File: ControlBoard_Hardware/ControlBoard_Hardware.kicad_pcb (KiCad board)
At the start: 2 copper layers, 96.5 x 66 mm, 52 parts, among them U10 MCP1415, U11 TSR_1-2450, U2 TSR_1-2450, U3 MCP1415, U4 OKI-78SR-12, U6 MCP1415, U7 MCP1415, U8 MCP1415, U9 MCP1415

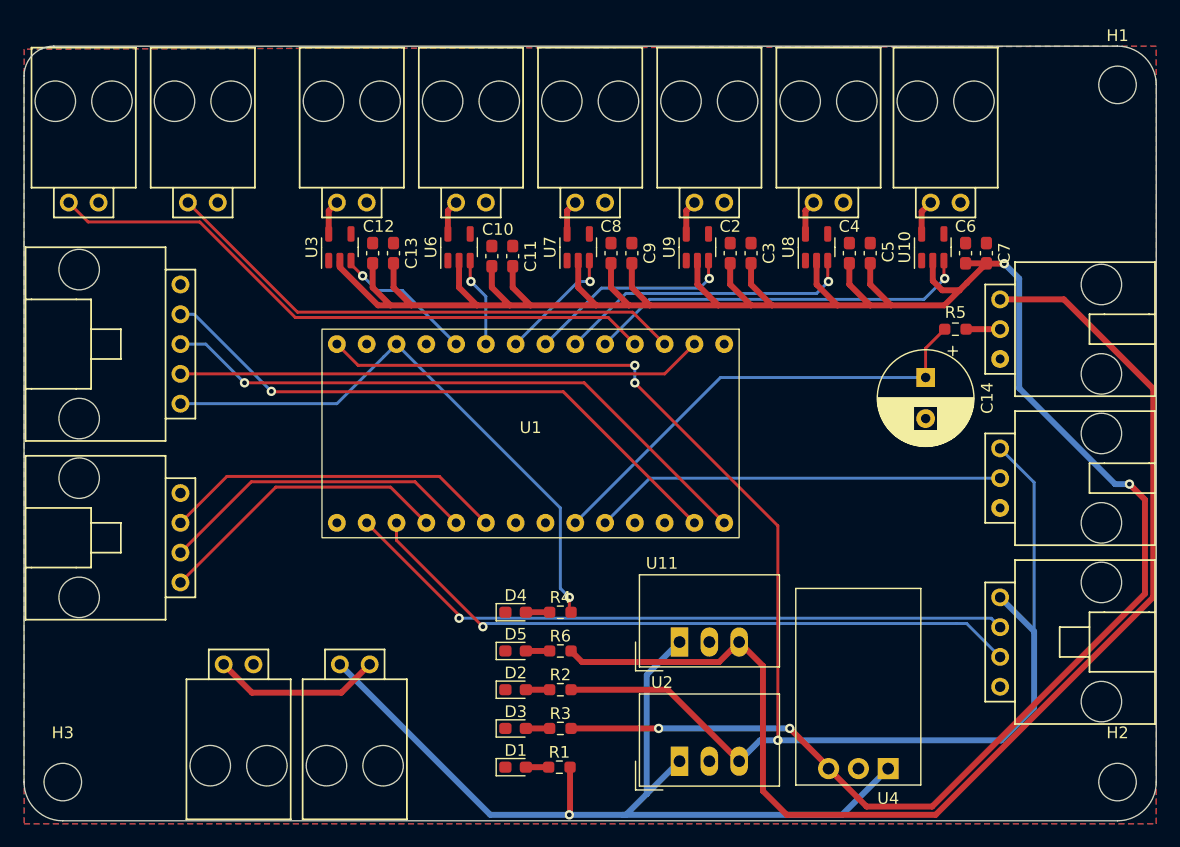
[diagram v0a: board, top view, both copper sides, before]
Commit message: Added silk screens
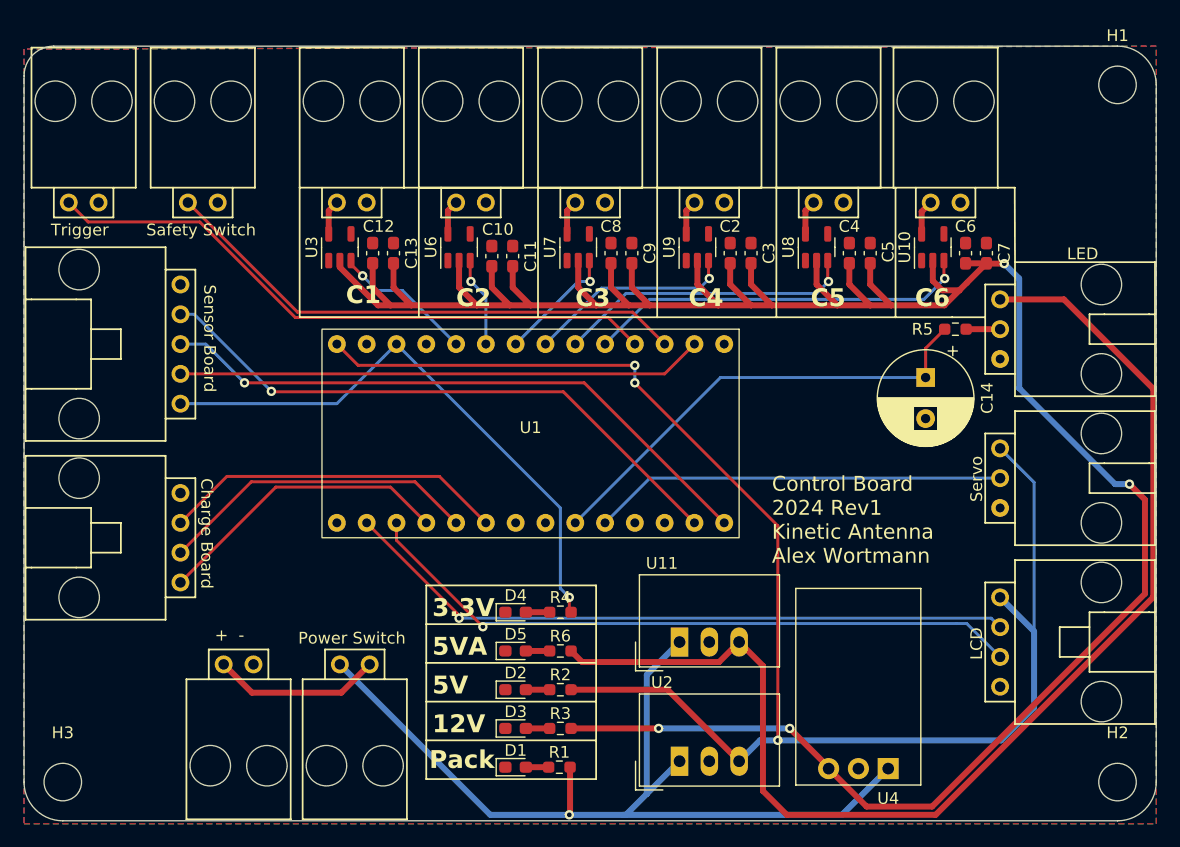
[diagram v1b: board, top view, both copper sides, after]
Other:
- board text added: "+ -"
- board text added: "12V"
- board text added: "3.3V"
- board text added: "5V"
- board text added: "5VA"
- board text added: "C1"
- board text added: "C2"
- board text added: "C3"
- board text added: "C4"
- board text added: "C5"
- board text added: "C6"
- board text added: "Charge Board"
- board text added: "Control Board 2024 Rev1 Kinetic Antenna Alex Wortmann"
- board text added: "LCD"
- board text added: "LED"
- board text added: "Pack"
- board text added: "Power Switch"
- board text added: "Safety Switch"
- board text added: "Sensor Board"
- board text added: "Servo"
- board text added: "Trigger"
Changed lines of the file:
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@@
     (property "ki_keywords" "R res resistor")
     (attr smd)
-    (fp_text reference "R5" (at 0 -1.43) (layer "F.SilkS")
+    (fp_text reference "R5" (at -2.8175 0) (layer "F.SilkS")
         (effects (font (size 1 1) (thickness 0.15)))
     )
@@
     )
   )
+  (gr_line (start 150.495 47.625) (end 150.495 58.674)
+    (stroke (width 0.15) (type default)) (layer "F.SilkS"))
+  (gr_line (start 170.815 47.625) (end 170.815 58.674)
+    (stroke (width 0.15) (type default)) (layer "F.SilkS"))
+  (gr_line (start 165.608 81.534) (end 151.13 81.534)
+    (stroke (width 0.15) (type default)) (layer "F.SilkS"))
+  (gr_line (start 165.608 98.044) (end 165.608 81.534)
+    (stroke (width 0.15) (type default)) (layer "F.SilkS"))
+  (gr_line (start 195.961 58.674) (end 198.755 58.674)
+    (stroke (width 0.15) (type default)) (layer "F.SilkS"))
+  (gr_line (start 165.608 94.742) (end 151.13 94.742)
+    (stroke (width 0.15) (type default)) (layer "F.SilkS"))
+  (gr_line (start 201.3185 53.975) (end 201.295 47.625)
+    (stroke (width 0.15) (type default)) (layer "F.SilkS"))
+  (gr_line (start 165.608 91.44) (end 151.13 91.44)
+    (stroke (width 0.15) (type default)) (layer "F.SilkS"))
+  (gr_line (start 199.848698 47.625) (end 201.295 47.625)
+    (stroke (width 0.15) (type default)) (layer "F.SilkS"))
+  (gr_line (start 165.608 88.138) (end 151.13 88.138)
+    (stroke (width 0.15) (type default)) (layer "F.SilkS"))
+  (gr_line (start 191.135 47.625) (end 191.135 58.674)
+    (stroke (width 0.15) (type default)) (layer "F.SilkS"))
+  (gr_line (start 150.495 58.674) (end 195.961 58.674)
+    (stroke (width 0.15) (type default)) (layer "F.SilkS"))
+  (gr_line (start 160.655 47.625) (end 160.655 58.674)
+    (stroke (width 0.15) (type default)) (layer "F.SilkS"))
+  (gr_line (start 190.958698 47.625) (end 149.225 47.625)
+    (stroke (width 0.15) (type default)) (layer "F.SilkS"))
+  (gr_line (start 140.335 47.625) (end 140.335 58.674)
+    (stroke (width 0.15) (type default)) (layer "F.SilkS"))
+  (gr_line (start 165.608 84.836) (end 151.13 84.836)
+    (stroke (width 0.15) (type default)) (layer "F.SilkS"))
+  (gr_line (start 151.13 81.534) (end 151.13 98.044)
+    (stroke (width 0.15) (type default)) (layer "F.SilkS"))
+  (gr_line (start 180.975 47.625) (end 180.975 58.674)
+    (stroke (width 0.15) (type default)) (layer "F.SilkS"))
+  (gr_line (start 150.495 58.674) (end 140.335 58.674)
+    (stroke (width 0.15) (type default)) (layer "F.SilkS"))
+  (gr_line (start 151.13 98.044) (end 165.608 98.044)
+    (stroke (width 0.15) (type default)) (layer "F.SilkS"))
   (gr_line (start 213.36 98.298) (end 213.36 38.862)
     (stroke (width 0.1) (type default)) (layer "Edge.Cuts"))
@@
   (gr_line (start 120.142 101.6) (end 210.058 101.6)
     (stroke (width 0.1) (type default)) (layer "Edge.Cuts"))
+  (gr_text "C4" (at 173.482 57.912) (layer "F.SilkS")
+    (effects (font (size 1.524 1.524) (thickness 0.254) bold) (justify left bottom))
+  )
+  (gr_text "12V" (at 151.638 94.234) (layer "F.SilkS")
+    (effects (font (size 1.524 1.524) (thickness 0.254) bold) (justify left bottom))
+  )
+  (gr_text "+  -" (at 133.096 86.36) (layer "F.SilkS")
+    (effects (font (size 1 1) (thickness 0.15)) (justify left bottom))
+  )
+  (gr_text "C6" (at 192.786 57.912) (layer "F.SilkS")
+    (effects (font (size 1.524 1.524) (thickness 0.254) bold) (justify left bottom))
+  )
+  (gr_text "Control Board\n2024 Rev1\nKinetic Antenna\nAlex Wortmann" (at 180.594 79.756) (layer "F.SilkS")
+    (effects (font (size 1.27 1.27) (thickness 0.15)) (justify left bottom))
+  )
+  (gr_text "Safety Switch" (at 127.254 51.816) (layer "F.SilkS")
+    (effects (font (size 1 1) (thickness 0.15)) (justify left bottom))
+  )
+  (gr_text "Charge Board" (at 131.826 72.39 -90) (layer "F.SilkS")
+    (effects (font (size 1 1) (thickness 0.15)) (justify left bottom))
+  )
+  (gr_text "Servo" (at 198.628 74.422 90) (layer "F.SilkS")
+    (effects (font (size 1 1) (thickness 0.15)) (justify left bottom))
+  )
+  (gr_text "LED" (at 205.74 53.848) (layer "F.SilkS")
+    (effects (font (size 1 1) (thickness 0.15)) (justify left bottom))
+  )
+  (gr_text "C3" (at 163.83 57.912) (layer "F.SilkS")
+    (effects (font (size 1.524 1.524) (thickness 0.254) bold) (justify left bottom))
+  )
+  (gr_text "5VA" (at 151.638 87.63) (layer "F.SilkS")
+    (effects (font (size 1.524 1.524) (thickness 0.254) bold) (justify left bottom))
+  )
+  (gr_text "5V" (at 151.638 90.932) (layer "F.SilkS")
+    (effects (font (size 1.524 1.524) (thickness 0.254) bold) (justify left bottom))
+  )
+  (gr_text "Sensor Board" (at 132.08 55.88 -90) (layer "F.SilkS")
+    (effects (font (size 1 1) (thickness 0.15)) (justify left bottom))
+  )
+  (gr_text "3.3V" (at 151.638 84.328) (layer "F.SilkS")
+    (effects (font (size 1.524 1.524) (thickness 0.254) bold) (justify left bottom))
+  )
+  (gr_text "LCD" (at 198.628 87.884 90) (layer "F.SilkS")
+    (effects (font (size 1 1) (thickness 0.15)) (justify left bottom))
+  )
+  (gr_text "Pack" (at 151.384 97.282) (layer "F.SilkS")
+    (effects (font (size 1.524 1.524) (thickness 0.254) bold) (justify left bottom))
+  )
+  (gr_text "C5" (at 183.896 57.912) (layer "F.SilkS")
+    (effects (font (size 1.524 1.524) (thickness 0.254) bold) (justify left bottom))
+  )
+  (gr_text "Trigger" (at 119.126 51.816) (layer "F.SilkS")
+    (effects (font (size 1 1) (thickness 0.15)) (justify left bottom))
+  )
+  (gr_text "Power Switch" (at 140.208 86.614) (layer "F.SilkS")
+    (effects (font (size 1 1) (thickness 0.15)) (justify left bottom))
+  )
+  (gr_text "C1" (at 144.272 57.658) (layer "F.SilkS")
+    (effects (font (size 1.524 1.524) (thickness 0.254) bold) (justify left bottom))
+  )
+  (gr_text "C2" (at 153.67 57.912) (layer "F.SilkS")
+    (effects (font (size 1.524 1.524) (thickness 0.254) bold) (justify left bottom))
+  )
   (dimension (type aligned) (layer "Dwgs.User")
     (pts (xy 210.058 38.862) (xy 210.058 98.298))

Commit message: ahhhhhhhh
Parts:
- removed PowerSwich1: Molex_SL_02, MRDT_Connectors:MOLEX_SL_02_Horizontal
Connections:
- C14 pad 1: LED Data -> +5VA
- Conn1 pad 2: Net-(Conn1-Pad2) -> /PWR_IN
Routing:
- net +5VA: track 104.7 -> 120.2 mm
- net Net-(Conn1-Pad2): track 14.4 -> 0.00 mm
- net /PWR_IN: track 78.6 -> 88.5 mm
- net LED Data: track 39.8 -> 38.3 mm, vias 0 -> 1
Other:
- board text removed: "Power Switch"

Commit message: yes
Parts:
- C10, C12, C2, C4, C6, C8: value 10uF -> 1uF
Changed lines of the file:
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@@
         (effects (font (size 1 1) (thickness 0.15)))
     )
-    (fp_text value "10uF" (at 0 1.43 90) (layer "F.Fab")
+    (fp_text value "1uF" (at 0 1.43 90) (layer "F.Fab")
         (effects (font (size 1 1) (thickness 0.15)))
     )
@@
         (effects (font (size 1 1) (thickness 0.15)))
     )
-    (fp_text value "10uF" (at 0 1.43 90) (layer "F.Fab")
+    (fp_text value "1uF" (at 0 1.43 90) (layer "F.Fab")
         (effects (font (size 1 1) (thickness 0.15)))
     )
@@
         (effects (font (size 1 1) (thickness 0.15)))
     )
-    (fp_text value "10uF" (at 0 1.43 90) (layer "F.Fab")
+    (fp_text value "1uF" (at 0 1.43 90) (layer "F.Fab")
         (effects (font (size 1 1) (thickness 0.15)))
     )
@@
         (effects (font (size 1 1) (thickness 0.15)))
     )
-    (fp_text value "10uF" (at 0 1.43 90) (layer "F.Fab")
+    (fp_text value "1uF" (at 0 1.43 90) (layer "F.Fab")
         (effects (font (size 1 1) (thickness 0.15)))
     )
@@
         (effects (font (size 1 1) (thickness 0.15)))
     )
-    (fp_text value "10uF" (at 0 1.43 90) (layer "F.Fab")
+    (fp_text value "1uF" (at 0 1.43 90) (layer "F.Fab")
         (effects (font (size 1 1) (thickness 0.15)))
     )
@@
         (effects (font (size 1 1) (thickness 0.15)))
     )
-    (fp_text value "10uF" (at 0 1.43 90) (layer "F.Fab")
-        (effects (font (size 1 1) (thickness 0.15)))
-    )
+    (fp_text value "1uF" (at 0 1.43 90) (layer "F.Fab")
+        (effects (font (size 1 1) (thickness 0.15)))
+    )

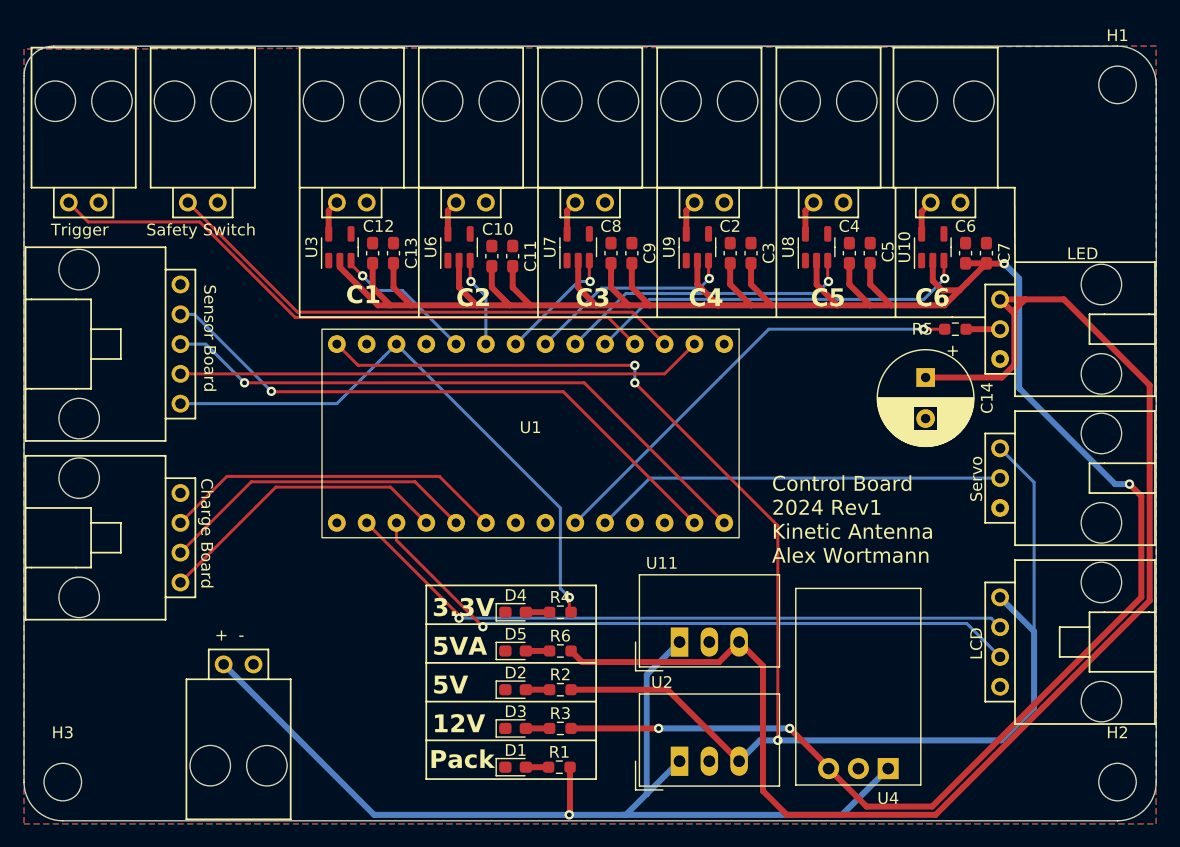
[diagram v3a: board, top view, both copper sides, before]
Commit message: changed review critiques
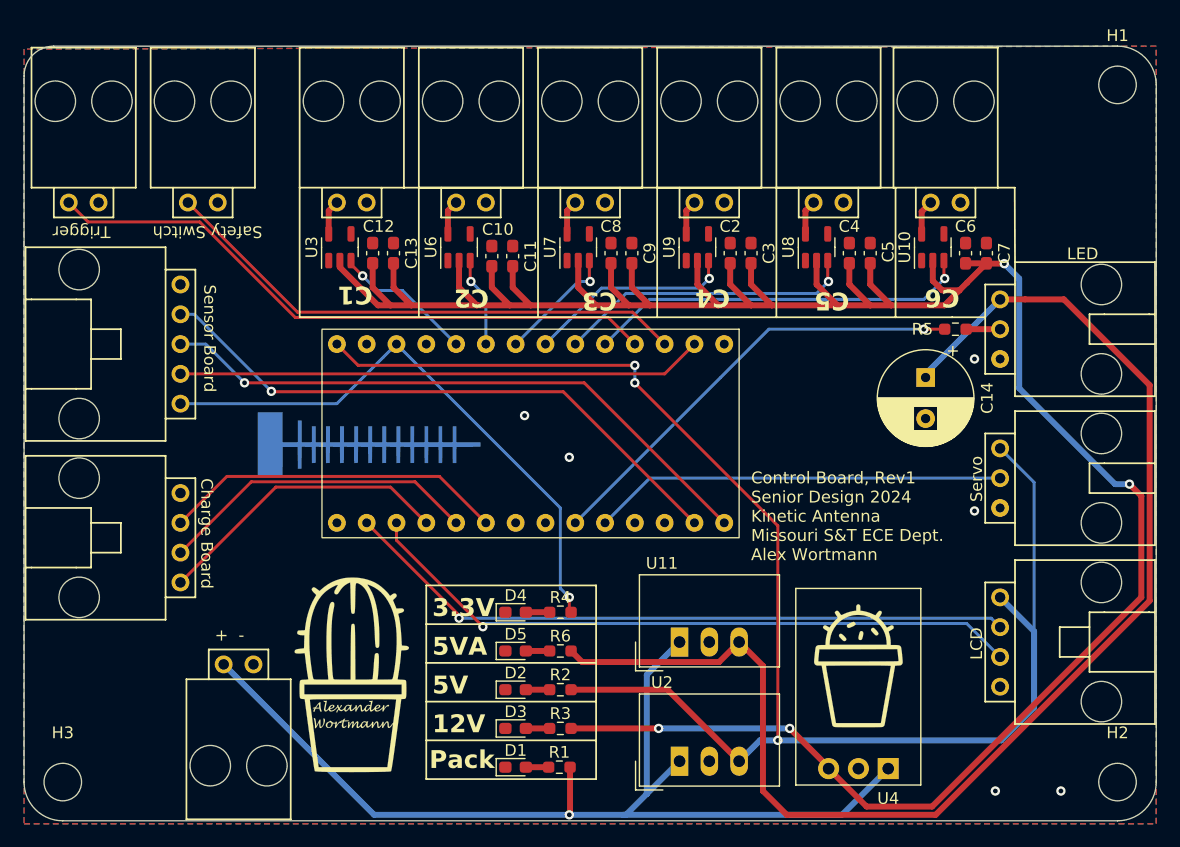
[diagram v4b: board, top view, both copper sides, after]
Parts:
- added G***: LOGO, MRDT_Silkscreens:z_sig_Alex_Wortmann_PT2, F.Cu at (188.0, 88.6)
- added G***: LOGO, MRDT_Silkscreens:z_sig_Alex_Wortmann_PT1, F.Cu at (144.8, 89.2)
- added G***: LOGO, MRDT_Silkscreens:yagi, B.Cu at (146.3, 69.6)
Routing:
- net +5VA: track 120.2 -> 113.8 mm
- net GND: vias 0 -> 6
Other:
- board text added: "Control Board, Rev1 Senior Design 2024 Kinetic Antenna Missouri S&T ECE Dept. Alex Wortmann"
- board text removed: "Control Board 2024 Rev1 Kinetic Antenna Alex Wortmann"
